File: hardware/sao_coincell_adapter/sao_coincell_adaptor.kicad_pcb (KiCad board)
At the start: 2 copper layers, 33.6 x 35.6 mm, 3 parts, among them J1 Conn_02x03_Odd_Even

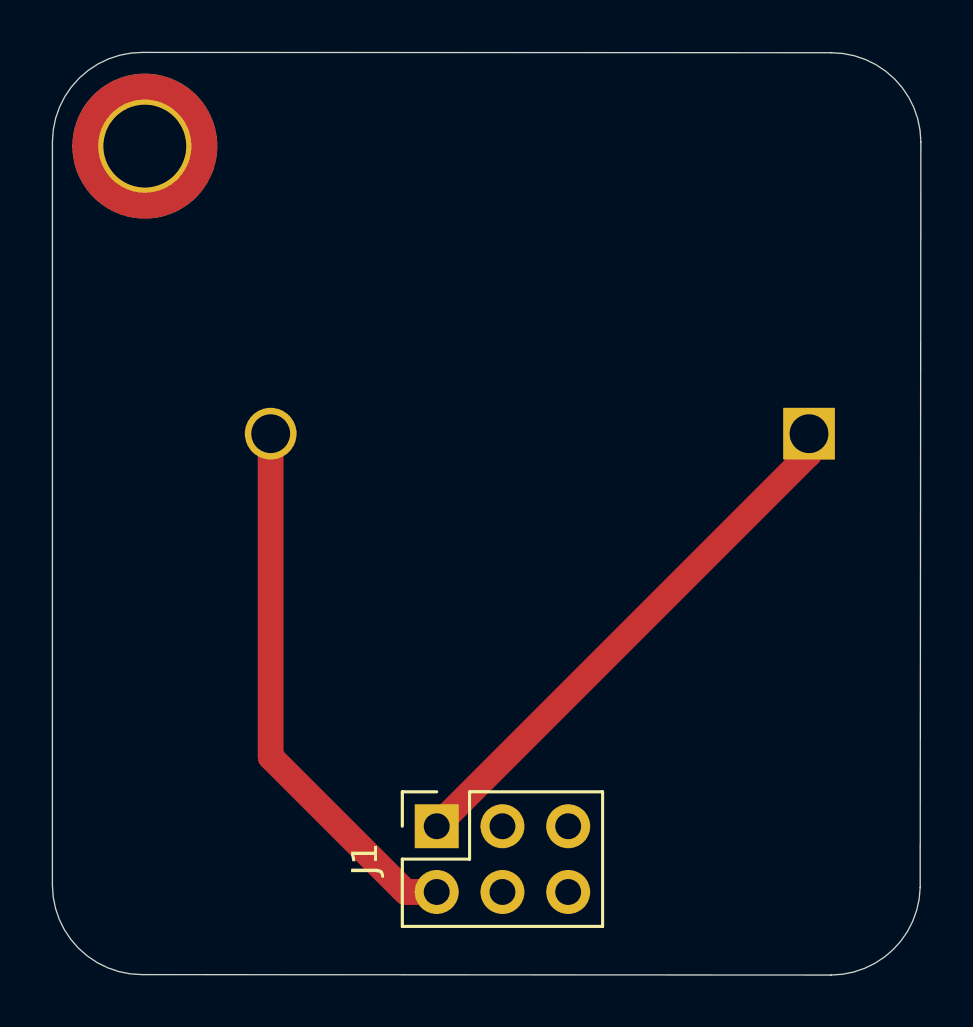
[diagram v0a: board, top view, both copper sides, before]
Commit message: Add hardware visual diff CI test
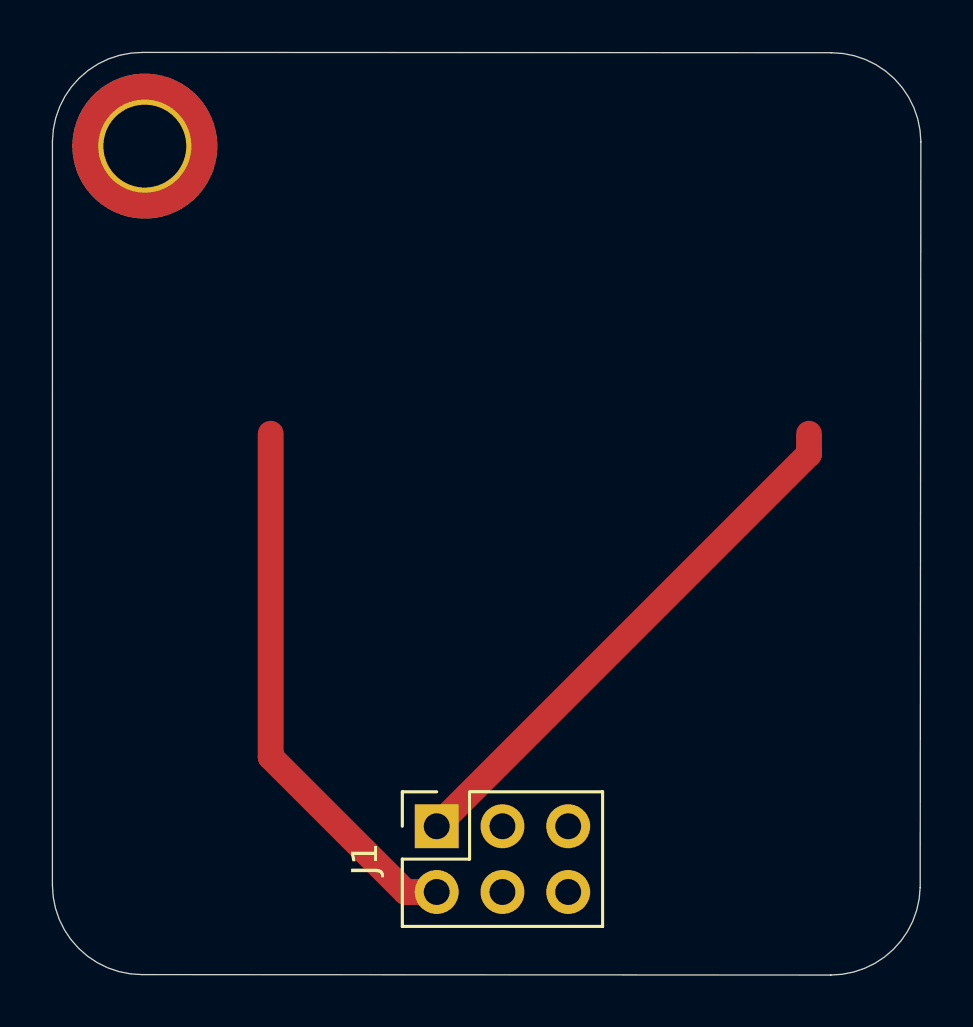
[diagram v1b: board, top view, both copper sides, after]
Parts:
- removed BT1: Battery, Battery:BatteryHolder_MYOUNG_BS-07-A1BJ001_CR2032
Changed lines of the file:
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@@
 		(embedded_fonts no)
-	)
-	(footprint "Battery:BatteryHolder_MYOUNG_BS-07-A1BJ001_CR2032"
-		(layer "B.Cu")
-		(at 174.66153 72.683197 180)
-		(descr "CR2032 battery holder https://www.lcsc.com/datasheet/lcsc_datasheet_2203021630_MYOUNG-BS-07-A1BJ001_C2979167.pdf")
-		(tags "CR2032 BR2032 BatteryHolder Battery")
-		(property "Reference" "BT1"
-			(at -1.5 4.2 0)
-			(unlocked yes)
-			(layer "B.SilkS")
-			(effects
-				(font
-					(size 1 1)
-					(thickness 0.15)
-				)
-				(justify mirror)
-			)
-		)
-		(property "Value" "Battery"
-			(at 12.4 -13 0)
-			(unlocked yes)
-			(layer "B.Fab")
-			(effects
-				(font
-					(size 1 1)
-					(thickness 0.15)
-				)
-				(justify mirror)
-			)
-		)
-		(property "Datasheet" ""
-			(at 12.4 0 0)
-			(unlocked yes)
-			(layer "B.Fab")
-			(hide yes)
-			(effects
-				(font
-					(size 1 1)
-					(thickness 0.15)
-				)
-				(justify mirror)
-			)
-		)
-		(property "Description" "Multiple-cell battery"
-			(at 12.4 0 180)
-			(unlocked yes)
-			(layer "B.Fab")
-			(hide yes)
-			(effects
-				(font
-					(size 1 1)
-					(thickness 0.15)
-				)
-				(justify mirror)
-			)
-		)
-		(sheetname "/")
-		(sheetfile "sao_coincell_adaptor.kicad_sch")
-		(attr through_hole)
-		(fp_line
-			(start 1.9 0.5)
-			(end 1.9 -0.5)
-			(stroke
-				(width 0.12)
-				(type default)
-			)
-			(layer "B.SilkS")
-		)
-		(fp_line
-			(start 1.4 0)
-			(end 2.4 0)
-			(stroke
-				(width 0.12)
-				(type default)
-			)
-			(layer "B.SilkS")
-		)
-		(fp_arc
-			(start 0.900001 -3.1)
-			(mid 24.310499 0)
-			(end 0.900001 3.1)
-			(stroke
-				(width 0.12)
-				(type default)
-			)
-			(layer "B.SilkS")
-		)
-		(fp_line
-			(start 0.65 -3.15)
-			(end -2.85 -3.15)
-			(stroke
-				(width 0.05)
-				(type default)
-			)
-			(layer "B.CrtYd")
-		)
-		(fp_line
-			(start -2.85 3.15)
-			(end 0.65 3.15)
-			(stroke
-				(width 0.05)
-				(type default)
-			)
-			(layer "B.CrtYd")
-		)
-		(fp_line
-			(start -2.85 -3.15)
-			(end -2.85 3.15)
-			(stroke
-				(width 0.05)
-				(type default)
-			)
-			(layer "B.CrtYd")
-		)
-		(fp_arc
-			(start 0.65 -3.15)
-			(mid 24.564907 0)
-			(end 0.65 3.15)
-			(stroke
-				(width 0.05)
-				(type default)
-			)
-			(layer "B.CrtYd")
-		)
-		(fp_line
-			(start -2.6 2.875)
-			(end 1.15 2.875)
-			(stroke
-				(width 0.1)
-				(type default)
-			)
-			(layer "B.Fab")
-		)
-		(fp_line
-			(start -2.6 2.875)
-			(end -2.6 -2.875)
-			(stroke
-				(width 0.1)
-				(type default)
-			)
-			(layer "B.Fab")
-		)
-		(fp_line
-			(start -2.6 -2.875)
-			(end 1.15 -2.875)
-			(stroke
-				(width 0.1)
-				(type default)
-			)
-			(layer "B.Fab")
-		)
-		(fp_circle
-			(center 12.4 0)
-			(end 24 0)
-			(stroke
-				(width 0.1)
-				(type default)
-			)
-			(fill no)
-			(layer "B.Fab")
-		)
-		(fp_text user "${REFERENCE}"
-			(at 12.4 0 0)
-			(unlocked yes)
-			(layer "B.Fab")
-			(effects
-				(font
-					(size 1 1)
-					(thickness 0.15)
-				)
-				(justify mirror)
-			)
-		)
-		(pad "1" thru_hole rect
-			(at 0 0)
-			(size 2 2)
-			(drill 1.5)
-			(layers "*.Cu" "*.Mask")
-			(remove_unused_layers no)
-			(net 4 "Net-(BT1-+)")
-			(pinfunction "+")
-			(pintype "passive")
-		)
-		(pad "2" thru_hole circle
-			(at 20.8 0)
-			(size 2 2)
-			(drill 1.5)
-			(layers "*.Cu" "*.Mask")
-			(remove_unused_layers no)
-			(net 5 "Net-(BT1--)")
-			(pinfunction "-")
-			(pintype "passive")
-		)
-		(embedded_fonts no)
-		(model "${KICAD9_3DMODEL_DIR}/Battery.3dshapes/BatteryHolder_MYOUNG_BS-07-A1BJ001_CR2032.wrl"
-			(offset
-				(xyz 0 0 0)
-			)
-			(scale
-				(xyz 1 1 1)
-			)
-			(rotate
-				(xyz 0 0 0)
-			)
-		)
 	)
 	(gr_arc

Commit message: Restore SAO coin cell holder
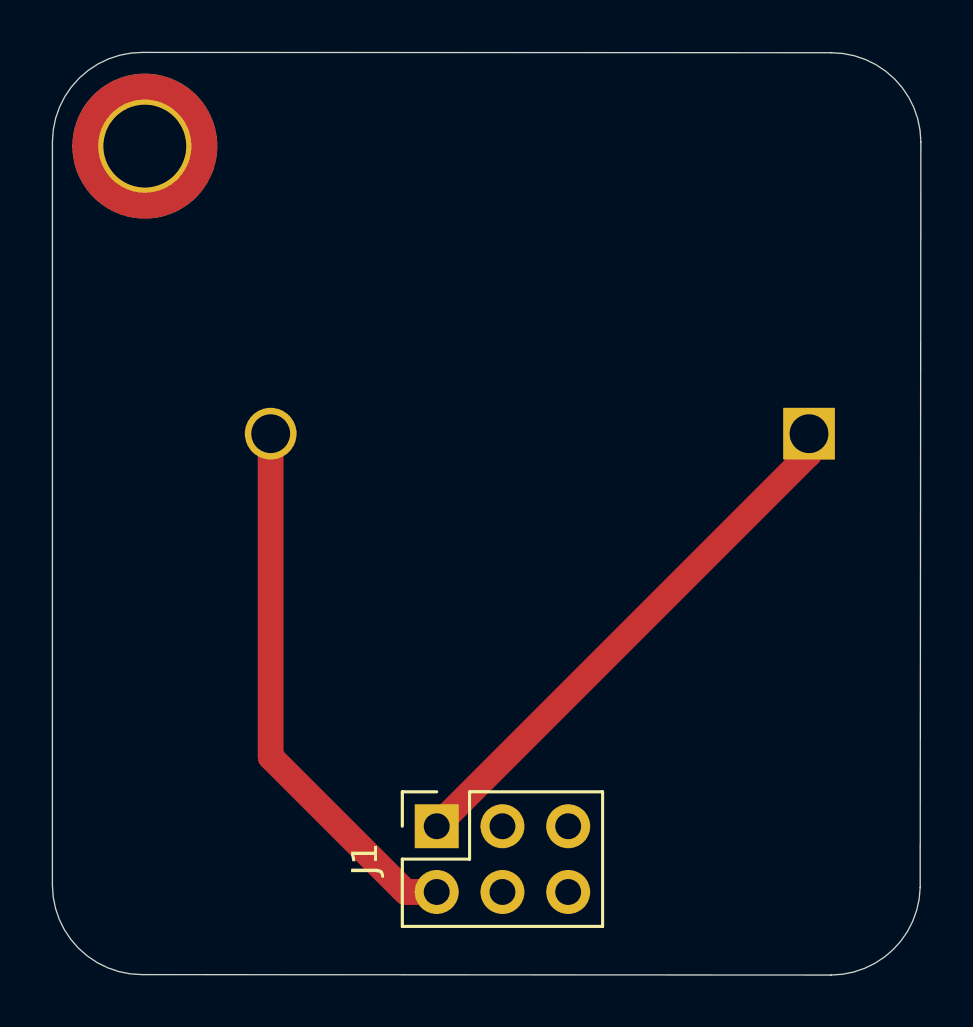
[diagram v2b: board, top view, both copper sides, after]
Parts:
- added BT1: Battery, Battery:BatteryHolder_MYOUNG_BS-07-A1BJ001_CR2032, B.Cu at (174.7, 72.7)
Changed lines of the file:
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@@
 		(embedded_fonts no)
+	)
+	(footprint "Battery:BatteryHolder_MYOUNG_BS-07-A1BJ001_CR2032"
+		(layer "B.Cu")
+		(at 174.66153 72.683197 180)
+		(descr "CR2032 battery holder https://www.lcsc.com/datasheet/lcsc_datasheet_2203021630_MYOUNG-BS-07-A1BJ001_C2979167.pdf")
+		(tags "CR2032 BR2032 BatteryHolder Battery")
+		(property "Reference" "BT1"
+			(at -1.5 4.2 0)
+			(unlocked yes)
+			(layer "B.SilkS")
+			(effects
+				(font
+					(size 1 1)
+					(thickness 0.15)
+				)
+				(justify mirror)
+			)
+		)
+		(property "Value" "Battery"
+			(at 12.4 -13 0)
+			(unlocked yes)
+			(layer "B.Fab")
+			(effects
+				(font
+					(size 1 1)
+					(thickness 0.15)
+				)
+				(justify mirror)
+			)
+		)
+		(property "Datasheet" ""
+			(at 12.4 0 0)
+			(unlocked yes)
+			(layer "B.Fab")
+			(hide yes)
+			(effects
+				(font
+					(size 1 1)
+					(thickness 0.15)
+				)
+				(justify mirror)
+			)
+		)
+		(property "Description" "Multiple-cell battery"
+			(at 12.4 0 180)
+			(unlocked yes)
+			(layer "B.Fab")
+			(hide yes)
+			(effects
+				(font
+					(size 1 1)
+					(thickness 0.15)
+				)
+				(justify mirror)
+			)
+		)
+		(sheetname "/")
+		(sheetfile "sao_coincell_adaptor.kicad_sch")
+		(attr through_hole)
+		(fp_line
+			(start 1.9 0.5)
+			(end 1.9 -0.5)
+			(stroke
+				(width 0.12)
+				(type default)
+			)
+			(layer "B.SilkS")
+		)
+		(fp_line
+			(start 1.4 0)
+			(end 2.4 0)
+			(stroke
+				(width 0.12)
+				(type default)
+			)
+			(layer "B.SilkS")
+		)
+		(fp_arc
+			(start 0.900001 -3.1)
+			(mid 24.310499 0)
+			(end 0.900001 3.1)
+			(stroke
+				(width 0.12)
+				(type default)
+			)
+			(layer "B.SilkS")
+		)
+		(fp_line
+			(start 0.65 -3.15)
+			(end -2.85 -3.15)
+			(stroke
+				(width 0.05)
+				(type default)
+			)
+			(layer "B.CrtYd")
+		)
+		(fp_line
+			(start -2.85 3.15)
+			(end 0.65 3.15)
+			(stroke
+				(width 0.05)
+				(type default)
+			)
+			(layer "B.CrtYd")
+		)
+		(fp_line
+			(start -2.85 -3.15)
+			(end -2.85 3.15)
+			(stroke
+				(width 0.05)
+				(type default)
+			)
+			(layer "B.CrtYd")
+		)
+		(fp_arc
+			(start 0.65 -3.15)
+			(mid 24.564907 0)
+			(end 0.65 3.15)
+			(stroke
+				(width 0.05)
+				(type default)
+			)
+			(layer "B.CrtYd")
+		)
+		(fp_line
+			(start -2.6 2.875)
+			(end 1.15 2.875)
+			(stroke
+				(width 0.1)
+				(type default)
+			)
+			(layer "B.Fab")
+		)
+		(fp_line
+			(start -2.6 2.875)
+			(end -2.6 -2.875)
+			(stroke
+				(width 0.1)
+				(type default)
+			)
+			(layer "B.Fab")
+		)
+		(fp_line
+			(start -2.6 -2.875)
+			(end 1.15 -2.875)
+			(stroke
+				(width 0.1)
+				(type default)
+			)
+			(layer "B.Fab")
+		)
+		(fp_circle
+			(center 12.4 0)
+			(end 24 0)
+			(stroke
+				(width 0.1)
+				(type default)
+			)
+			(fill no)
+			(layer "B.Fab")
+		)
+		(fp_text user "${REFERENCE}"
+			(at 12.4 0 0)
+			(unlocked yes)
+			(layer "B.Fab")
+			(effects
+				(font
+					(size 1 1)
+					(thickness 0.15)
+				)
+				(justify mirror)
+			)
+		)
+		(pad "1" thru_hole rect
+			(at 0 0)
+			(size 2 2)
+			(drill 1.5)
+			(layers "*.Cu" "*.Mask")
+			(remove_unused_layers no)
+			(net 4 "Net-(BT1-+)")
+			(pinfunction "+")
+			(pintype "passive")
+		)
+		(pad "2" thru_hole circle
+			(at 20.8 0)
+			(size 2 2)
+			(drill 1.5)
+			(layers "*.Cu" "*.Mask")
+			(remove_unused_layers no)
+			(net 5 "Net-(BT1--)")
+			(pinfunction "-")
+			(pintype "passive")
+		)
+		(embedded_fonts no)
+		(model "${KICAD9_3DMODEL_DIR}/Battery.3dshapes/BatteryHolder_MYOUNG_BS-07-A1BJ001_CR2032.wrl"
+			(offset
+				(xyz 0 0 0)
+			)
+			(scale
+				(xyz 1 1 1)
+			)
+			(rotate
+				(xyz 0 0 0)
+			)
+		)
 	)
 	(gr_arc
